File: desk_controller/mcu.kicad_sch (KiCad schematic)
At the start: 30 parts

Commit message: Added components
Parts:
- removed R? (x2): R, symbol Device:R
- removed U? (x2): PC817, Package_DIP:DIP-4_W7.62mm, symbol Isolator:PC817
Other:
- note removed: "optos are APC-817D1-SL"

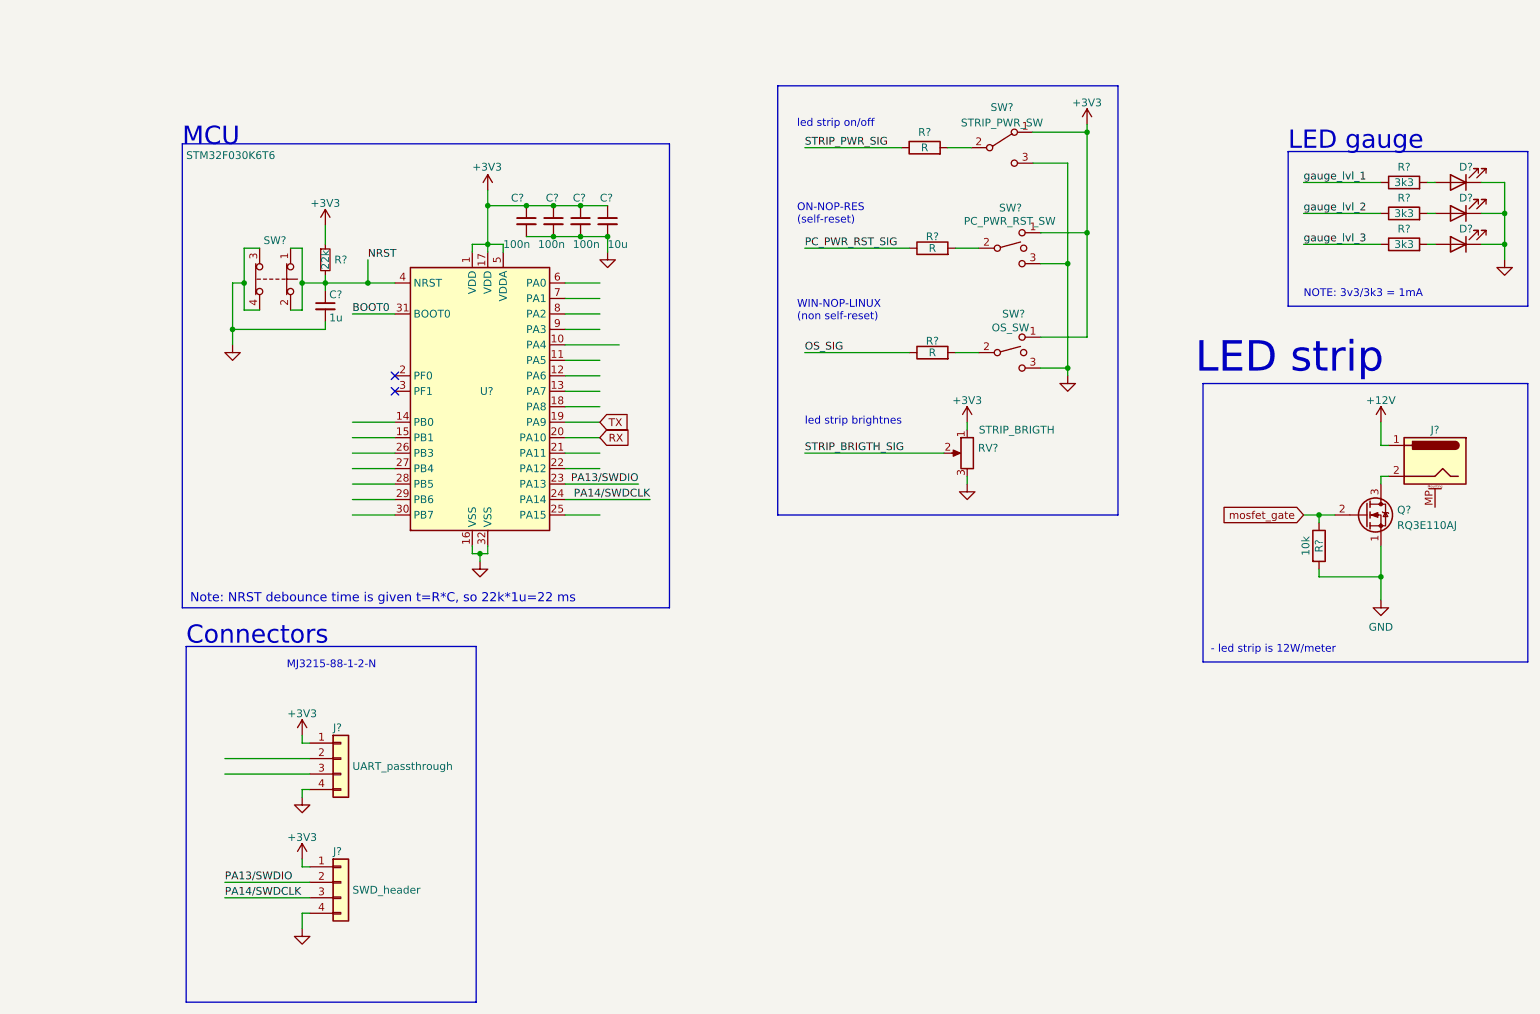
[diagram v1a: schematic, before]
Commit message: Buck converter sch, rs232 transceiver
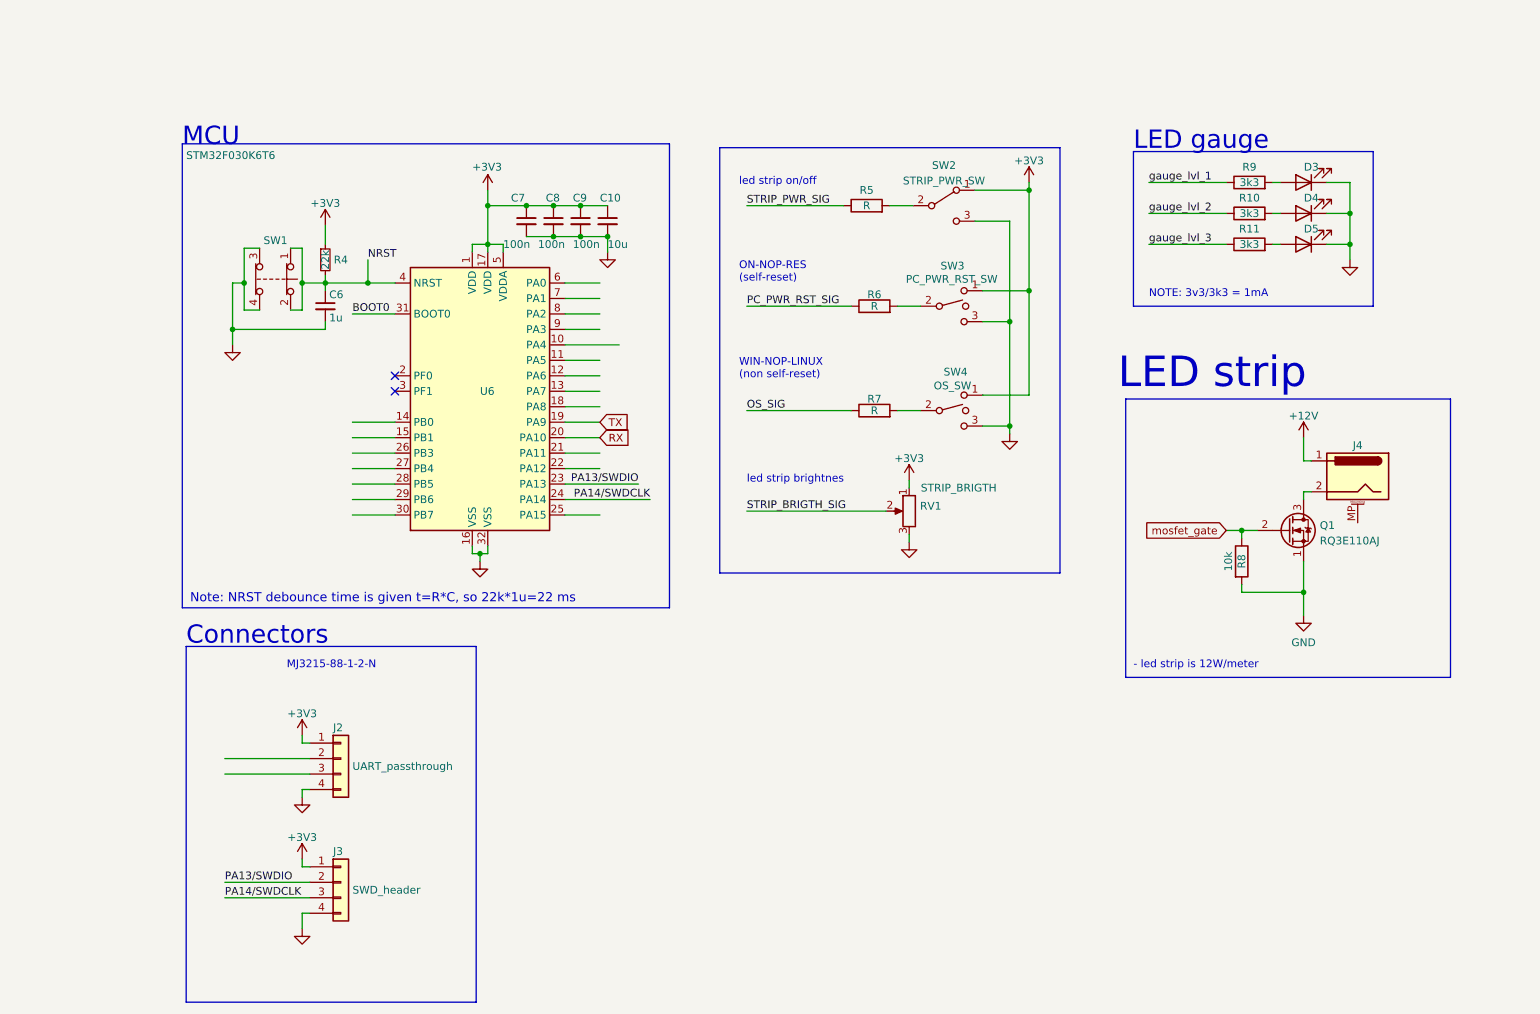
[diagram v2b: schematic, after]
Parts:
- gave numbers to parts that had none: 26
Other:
- moved on the sheet: D3, D4, D5, J4, Q1, R10, R11, R5, R6, R7, R8, R9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

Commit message: Sch fixes, initial board layout
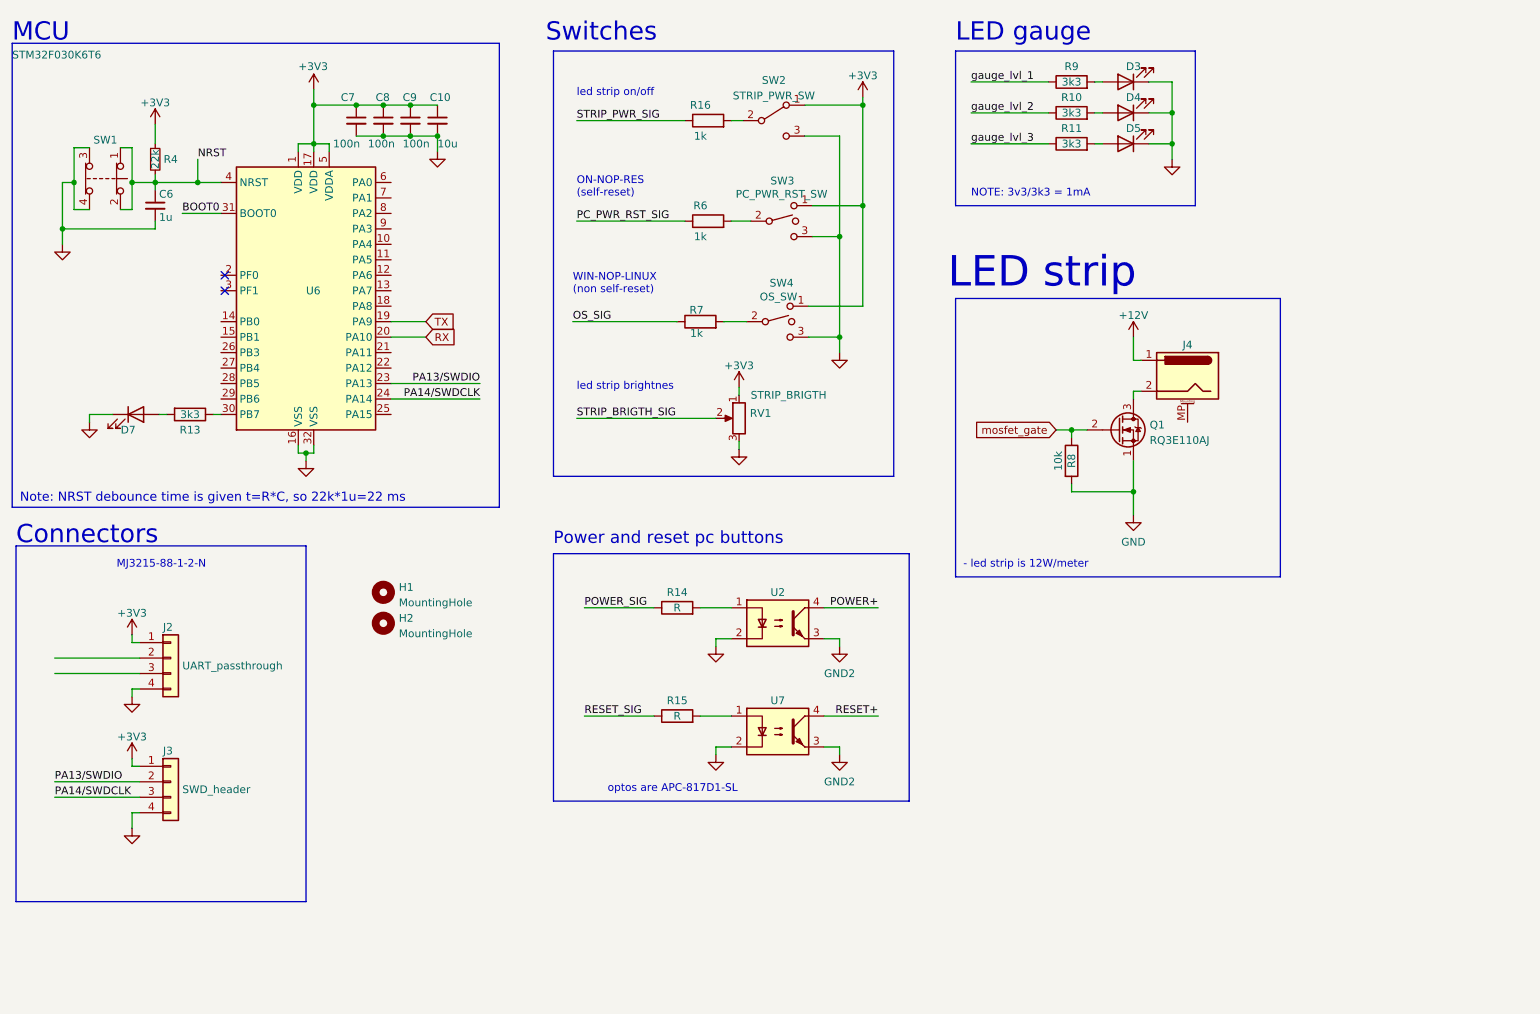
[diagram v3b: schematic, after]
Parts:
- removed R5: R, symbol Device:R
- added D7: RED, LED_SMD:LED_0603_1608Metric, symbol Device:LED
- added H1, H2: MountingHole, MountingHole:MountingHole_3.2mm_M3_Pad_TopBottom, symbol Mechanical:MountingHole
- added R13: 3k3, Resistor_SMD:R_0603_1608Metric, symbol Device:R
- added R14, R15: R, Resistor_SMD:R_0603_1608Metric, symbol Device:R
- added R16: 1k, Resistor_SMD:R_0603_1608Metric, symbol Device:R
- added U2, U7: PC817, Package_DIP:DIP-4_W7.62mm, symbol Isolator:PC817
- R6, R7: value R -> 1k; footprint (none) -> Resistor_SMD:R_0603_1608Metric
- RV1: footprint (none) -> Potentiometer_THT:Potentiometer_Alps_RK09K_Single_Vertical
- SW2, SW3, SW4: footprint (none) -> MTS-102-103:MTS-102-103
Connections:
- net GND: now also D7.1 (K), U2.2, U7.2
- net STRIP_PWR_SIG: now also R16.1
- net at U6.30 (PB7): now also R13.1
- net at SW2.2 (B): now also R16.2
- new net: R14.2, U2.1
- new net: R15.2, U7.1
- new net: D7.2 (A), R13.2
- new net GND2: U2.3, U7.3
- new net POWER+: U2.4
- new net POWER_SIG: R14.1
- new net RESET+: U7.4
- new net RESET_SIG: R15.1
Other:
- note added: "Power and reset pc buttons"
- note added: "Switches"
- note added: "optos are APC-817D1-SL"
- moved on the sheet: C10, C6, C7, C8, C9, D3, D4, D5, J2, J3, J4, Q1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

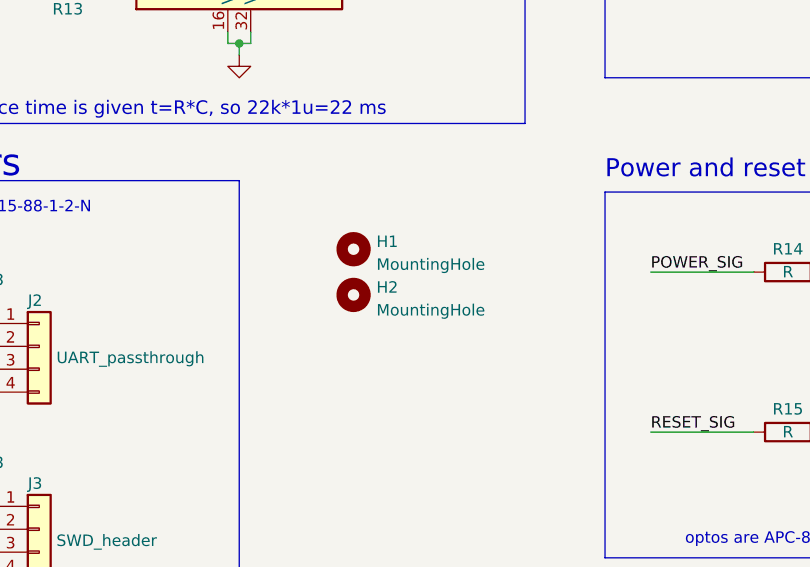
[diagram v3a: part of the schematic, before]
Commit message: Removed acdc brick
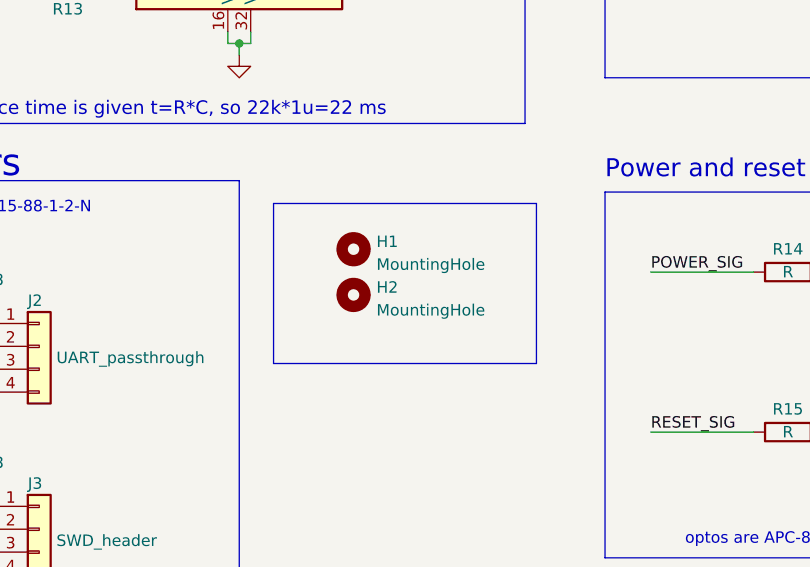
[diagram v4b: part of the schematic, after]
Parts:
- J4: footprint (none) -> Connector_BarrelJack:BarrelJack_GCT_DCJ200-10-A_Horizontal
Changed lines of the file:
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@@
+    (stroke (width 0) (type default) (color 0 0 0 0))
+  )
+  (polyline (pts (xy 71.12 104.14) (xy 71.12 121.92))
     (stroke (width 0) (type default) (color 0 0 0 0))
   )
@@
     (stroke (width 0) (type default) (color 0 0 0 0))
   )
+  (polyline (pts (xy 100.33 121.92) (xy 71.12 121.92))
+    (stroke (width 0) (type default) (color 0 0 0 0))
+  )
   (wire (pts (xy 66.04 86.36) (xy 67.31 86.36))
     (stroke (width 0) (type default) (color 0 0 0 0))
@@
     (stroke (width 0) (type default) (color 0 0 0 0))
   )
+  (polyline (pts (xy 71.12 104.14) (xy 100.33 104.14))
+    (stroke (width 0) (type default) (color 0 0 0 0))
+  )
   (wire (pts (xy 203.2 76.2) (xy 204.47 76.2))
     (stroke (width 0) (type default) (color 0 0 0 0))
@@
   )
   (wire (pts (xy 209.55 30.48) (xy 209.55 35.56))
+    (stroke (width 0) (type default) (color 0 0 0 0))
+  )
+  (polyline (pts (xy 100.33 104.14) (xy 100.33 121.92))
     (stroke (width 0) (type default) (color 0 0 0 0))
   )
@@
       (effects (font (size 1.27 1.27)) hide)
     )
-    (property "Footprint" "" (id 2) (at 210.82 74.676 0)
-      (effects (font (size 1.27 1.27)) hide)
-    )
+    (property "Footprint" "Connector_BarrelJack:BarrelJack_GCT_DCJ200-10-A_Horizontal" (id 2) (at 210.82 74.676 0)
+      (effects (font (size 1.27 1.27)) hide)
+    )

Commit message: Much progress in sch and brd
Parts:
- removed J2: UART_passthrough, Connector_PinHeader_2.54mm:PinHeader_1x04_P2.54mm_Vertical, symbol Connector_Generic:Conn_01x04
- removed R16: 1k, Resistor_SMD:R_0603_1608Metric, symbol Device:R
- removed RV1: STRIP_BRIGTH, Potentiometer_THT:Potentiometer_Alps_RK09K_Single_Vertical, symbol Device:R_Potentiometer
- removed SW2: STRIP_PWR_SW, MTS-102-103:MTS-102-103, symbol Switch:SW_SPDT
- added SW2: RotaryEncoder, Rotary_Encoder:RotaryEncoder_Alps_EC12E_Vertical_H20mm, symbol Device:RotaryEncoder
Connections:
- net TTL_TX_ISO: now reaches U6.10 (PA4)
- net TTL_DTR_ISO: now reaches U6.11 (PA5)
- net TTL_RTS_ISO: now reaches U6.12 (PA6)
- net TTL_RX_ISO: now reaches U6.13 (PA7)
- net GND2 renamed PC_GND
- net POWER+ renamed POWER
- net RESET+ renamed RESET
- no-connect marks 2 -> 3
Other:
- note added: "-U2 and U7 are APC-817D1-SL"
- note removed: "led strip on/off"
- note removed: "optos are APC-817D1-SL"
- moved on the sheet: C6, H1, H2, J3, J4, Q1, R14, R15, R4, R6, R7, R8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
